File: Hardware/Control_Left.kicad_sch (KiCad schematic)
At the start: 28 parts, among them J1 BAT, J2 JTAG, J3 1.08_MIP_MODULE, Q1 AO3401A, SW1 MSK12C02, SW2 SW_Push, U1 TPS61040DBV, U2 XIAO-NRF52840-PLUS

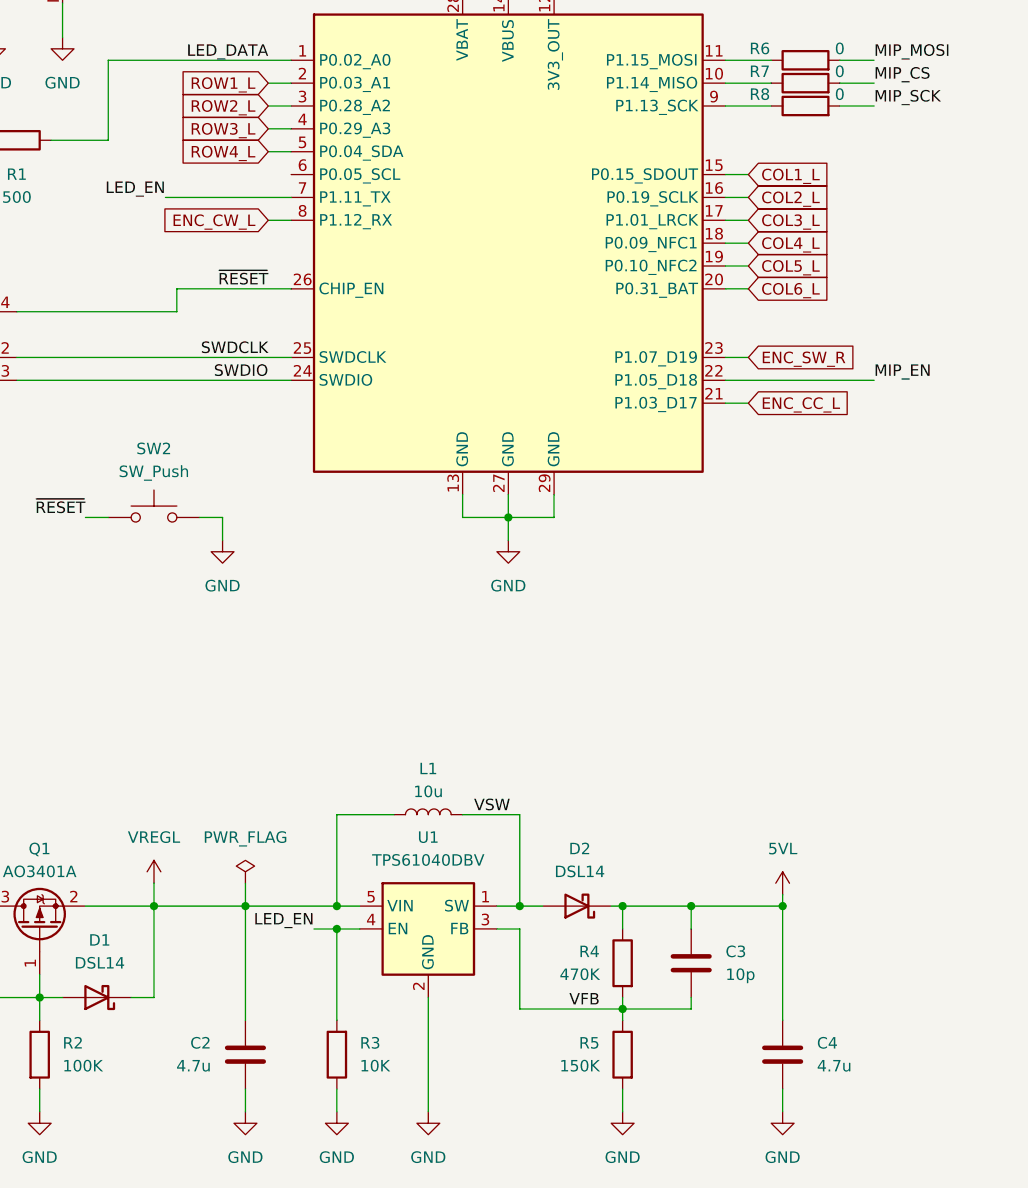
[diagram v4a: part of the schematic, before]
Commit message: Display model and layout
Updated the 3D model and footprint for the MIP display. It now sits further from the PCB.
Continued the layout and routing of the left side PCB.
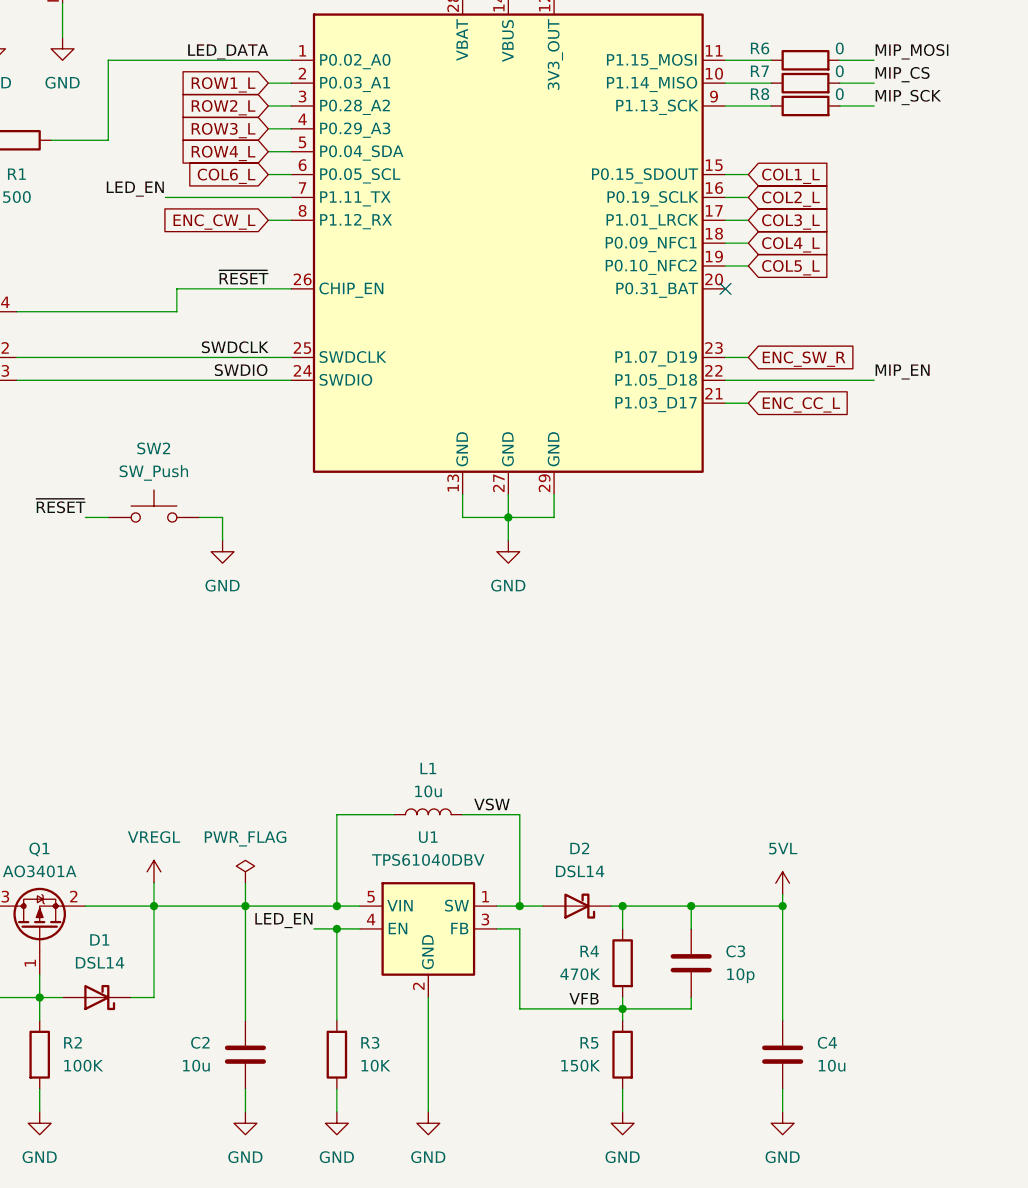
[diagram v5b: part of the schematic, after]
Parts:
- C2, C4: value 4.7u -> 10u; footprint Capacitor_SMD:C_1206_3216Metric -> Capacitor_SMD:C_0603_1608Metric; JLC Part C29823 -> C96446; Manufacturer Part 1206B475K500NT -> CL10A106MA8NRNC
- J3: footprint Custom_Parts:1.08_MIP_MODULE -> Custom_Parts:1.08_MIP_MODULE_TALL
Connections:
- net COL6_L: now also U2.6 (P0.05_SCL); no longer U2.20 (P0.31_BAT)
- no-connect marks 1 -> 2
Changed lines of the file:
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@@
 	)
 	(no_connect
+		(at 138.43 78.74)
+	)
+	(no_connect
 		(at 69.85 43.18)
 	)
@@
 	(wire
 		(pts
+			(xy 87.63 66.04) (xy 90.17 66.04)
+		)
+		(stroke
+			(width 0)
+			(type default)
+		)
+	)
+	(wire
+		(pts
 			(xy 69.85 62.23) (xy 69.85 53.34)
 		)
@@
 	(wire
 		(pts
-			(xy 138.43 78.74) (xy 140.97 78.74)
-		)
-		(stroke
-			(width 0)
-			(type default)
-		)
-	)
-	(wire
-		(pts
 			(xy 217.17 111.76) (xy 234.95 111.76)
 		)
@@
 		)
 	)
-	(global_label "COL6_L"
+	(global_label "ENC_CC_L"
 		(shape input)
-		(at 140.97 78.74 0)
+		(at 140.97 91.44 0)
 		(fields_autoplaced yes)
 		(effects
@@
 		)
 		(property "Intersheetrefs" "${INTERSHEET_REFS}"
-			(at 150.789 78.74 0)
+			(at 153.3894 91.44 0)
 			(hide yes)
 			(show_name no)
@@
 		)
 	)
-	(global_label "ENC_CC_L"
+	(global_label "ROW2_L"
 		(shape input)
-		(at 140.97 91.44 0)
+		(at 87.63 58.42 180)
 		(fields_autoplaced yes)
 		(effects
@@
 				(size 1.27 1.27)
 			)
-			(justify left)
+			(justify right)
 		)
 		(property "Intersheetrefs" "${INTERSHEET_REFS}"
-			(at 153.3894 91.44 0)
+			(at 77.811 58.42 0)
 			(hide yes)
 			(show_name no)
@@
 					(size 1.27 1.27)
 				)
-				(justify left)
+				(justify right)
 			)
 		)
 	)
-	(global_label "ROW2_L"
+	(global_label "ROW4_L"
 		(shape input)
-		(at 87.63 58.42 180)
+		(at 87.63 63.5 180)
 		(fields_autoplaced yes)
 		(effects
@@
 		)
 		(property "Intersheetrefs" "${INTERSHEET_REFS}"
-			(at 77.811 58.42 0)
+			(at 77.811 63.5 0)
 			(hide yes)
 			(show_name no)
@@
 		)
 	)
-	(global_label "ROW4_L"
+	(global_label "ENC_SW_R"
 		(shape input)
-		(at 87.63 63.5 180)
+		(at 140.97 86.36 0)
 		(fields_autoplaced yes)
 		(effects
@@
 				(size 1.27 1.27)
 			)
-			(justify right)
+			(justify left)
 		)
 		(property "Intersheetrefs" "${INTERSHEET_REFS}"
-			(at 77.811 63.5 0)
+			(at 153.5708 86.36 0)
 			(hide yes)
 			(show_name no)
@@
 					(size 1.27 1.27)
 				)
-				(justify right)
+				(justify left)
 			)
 		)
 	)
-	(global_label "ENC_SW_R"
+	(global_label "COL6_L"
 		(shape input)
-		(at 140.97 86.36 0)
+		(at 87.63 66.04 180)
 		(fields_autoplaced yes)
 		(effects
@@
 				(size 1.27 1.27)
 			)
-			(justify left)
+			(justify right)
 		)
 		(property "Intersheetrefs" "${INTERSHEET_REFS}"
-			(at 153.5708 86.36 0)
+			(at 77.811 66.04 0)
 			(hide yes)
 			(show_name no)
@@
 					(size 1.27 1.27)
 				)
-				(justify left)
+				(justify right)
 			)
 		)
@@
 			)
 		)
-		(property "Value" "4.7u"
+		(property "Value" "10u"
 			(at 81.28 165.0999 0)
 			(show_name no)
@@
 			)
 		)
-		(property "Footprint" "Capacitor_SMD:C_1206_3216Metric"
+		(property "Footprint" "Capacitor_SMD:C_0603_1608Metric"
 			(at 84.1248 167.64 0)
 			(hide yes)
@@
 			)
 		)
-		(property "JLC Part" "C29823"
+		(property "JLC Part" "C96446"
 			(at 85.09 163.83 0)
 			(hide yes)
@@
 			)
 		)
-		(property "Manufacturer Part" "1206B475K500NT"
+		(property "Manufacturer Part" "CL10A106MA8NRNC"
 			(at 85.09 163.83 0)
 			(hide yes)
@@
 			)
 		)
-		(property "Footprint" "Custom_Parts:1.08_MIP_MODULE"
+		(property "Footprint" "Custom_Parts:1.08_MIP_MODULE_TALL"
 			(at 238.76 120.65 0)
 			(hide yes)
@@
 			)
 		)
-		(property "Value" "4.7u"
+		(property "Value" "10u"
 			(at 148.59 165.0999 0)
 			(show_name no)
@@
 			)
 		)
-		(property "Footprint" "Capacitor_SMD:C_1206_3216Metric"
+		(property "Footprint" "Capacitor_SMD:C_0603_1608Metric"
 			(at 145.7452 167.64 0)
 			(hide yes)
@@
 			)
 		)
-		(property "JLC Part" "C29823"
+		(property "JLC Part" "C96446"
 			(at 144.78 163.83 0)
 			(hide yes)
@@
 			)
 		)
-		(property "Manufacturer Part" "1206B475K500NT"
+		(property "Manufacturer Part" "CL10A106MA8NRNC"
 			(at 144.78 163.83 0)
 			(hide yes)

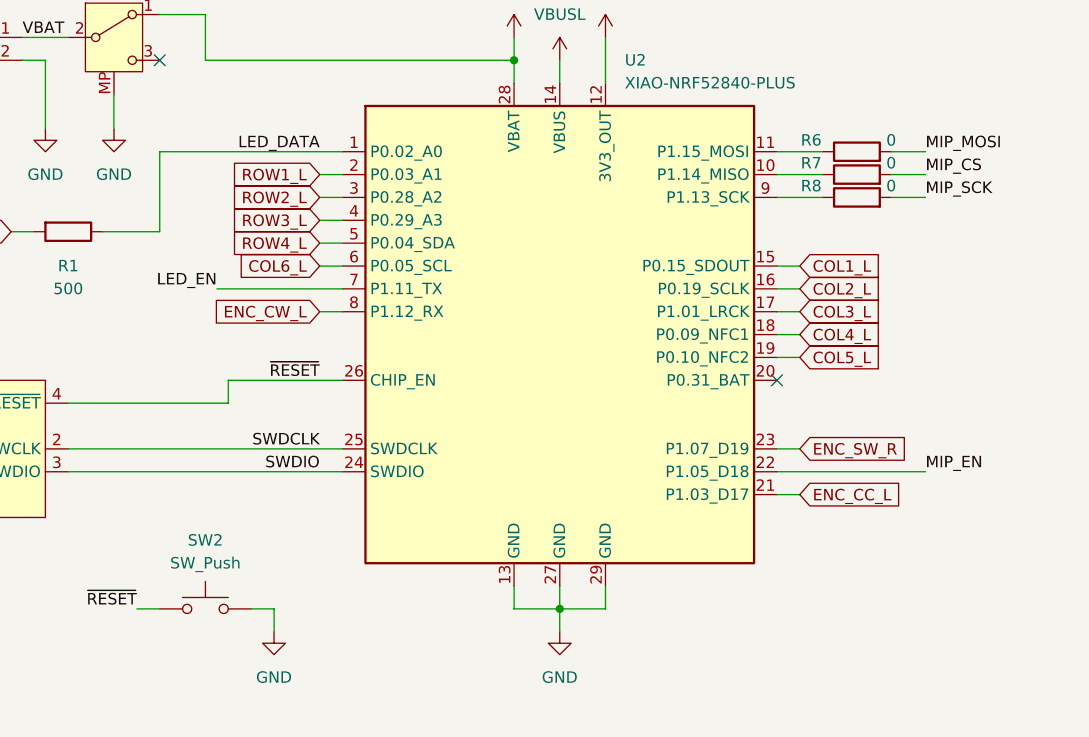
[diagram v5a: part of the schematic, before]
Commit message: Matrix routing and data lines
Routed some of the lines for the switch matrix.
Routed the singal lines for the MIP display.
Need to check clearenaces and spacing between the SPI lines.
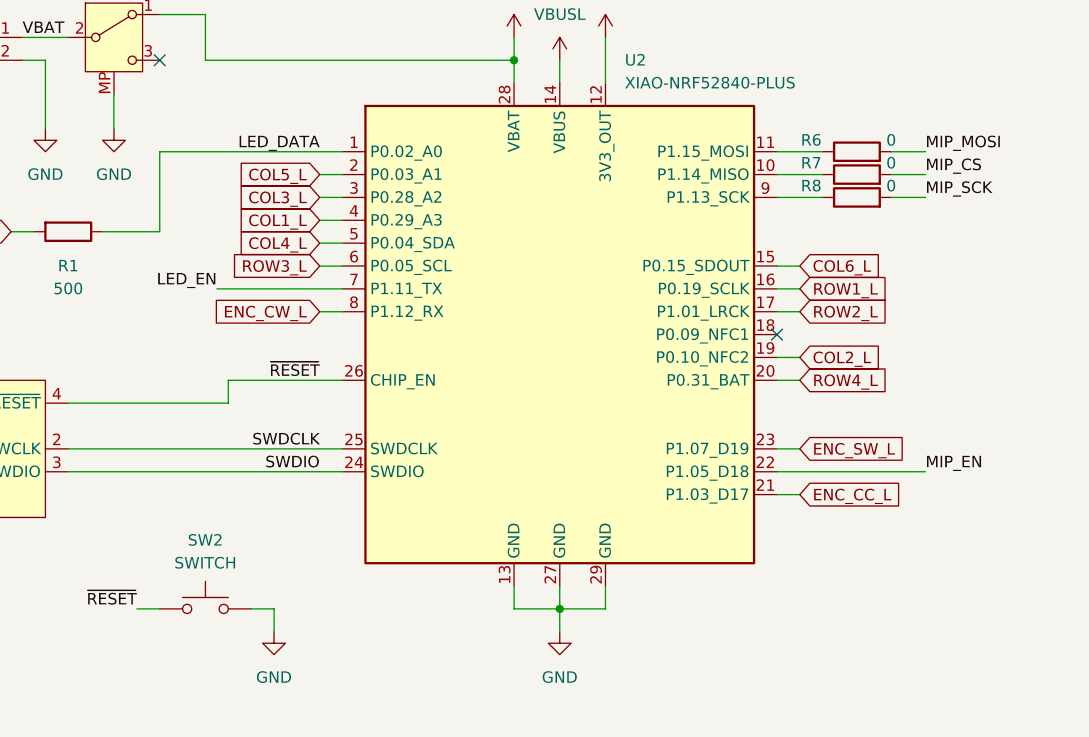
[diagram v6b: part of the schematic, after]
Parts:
- J1: footprint Custom_Parts:JST_PH_1x02_P2.00MM_SMD_HOR -> Custom_Parts:JST_ZH_1x02_P1.50MM_SMD_HORIZONTAL; JLC Part C3029440 -> C722913; Manufacturer Part WAFER-PH2.0-2PWB -> ZH1.5-2P-WT
- SW2: value SW_Push -> SWITCH
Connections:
- net COL1_L: now also U2.4 (P0.29_A3); no longer U2.15 (P0.15_SDOUT)
- net COL2_L: now also U2.19 (P0.10_NFC2); no longer U2.16 (P0.19_SCLK)
- net COL3_L: now also U2.3 (P0.28_A2); no longer U2.17 (P1.01_LRCK)
- net COL4_L: now also U2.5 (P0.04_SDA); no longer U2.18 (P0.09_NFC1)
- net COL5_L: now also U2.2 (P0.03_A1); no longer U2.19 (P0.10_NFC2)
- net COL6_L: now also U2.15 (P0.15_SDOUT); no longer U2.6 (P0.05_SCL)
- net ROW1_L: now also U2.16 (P0.19_SCLK); no longer U2.2 (P0.03_A1)
- net ROW2_L: now also U2.17 (P1.01_LRCK); no longer U2.3 (P0.28_A2)
- net ROW3_L: now also U2.6 (P0.05_SCL); no longer U2.4 (P0.29_A3)
- net ROW4_L: now also U2.20 (P0.31_BAT); no longer U2.5 (P0.04_SDA)
- net ENC_SW_R renamed ENC_SW_L
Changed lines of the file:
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@@
 	)
 	(no_connect
-		(at 138.43 78.74)
+		(at 138.43 73.66)
 	)
 	(no_connect
@@
 	(wire
 		(pts
-			(xy 140.97 73.66) (xy 138.43 73.66)
-		)
-		(stroke
-			(width 0)
-			(type default)
-		)
-	)
-	(wire
-		(pts
 			(xy 54.61 43.18) (xy 57.15 43.18)
 		)
@@
 		)
 	)
+	(wire
+		(pts
+			(xy 138.43 78.74) (xy 140.97 78.74)
+		)
+		(stroke
+			(width 0)
+			(type default)
+		)
+	)
 	(label "MIP_CS"
 		(at 154.94 55.88 0)
@@
 		)
 	)
-	(global_label "ROW1_L"
+	(global_label "ENC_CW_L"
 		(shape input)
-		(at 87.63 55.88 180)
+		(at 87.63 71.12 180)
 		(fields_autoplaced yes)
 		(effects
@@
 		)
 		(property "Intersheetrefs" "${INTERSHEET_REFS}"
-			(at 77.811 55.88 0)
+			(at 75.2106 71.12 0)
 			(hide yes)
 			(show_name no)
@@
 		)
 	)
-	(global_label "ENC_CW_L"
+	(global_label "ENC_CC_L"
 		(shape input)
-		(at 87.63 71.12 180)
+		(at 140.97 91.44 0)
 		(fields_autoplaced yes)
 		(effects
@@
 				(size 1.27 1.27)
 			)
-			(justify right)
+			(justify left)
 		)
 		(property "Intersheetrefs" "${INTERSHEET_REFS}"
-			(at 75.2106 71.12 0)
+			(at 153.3894 91.44 0)
 			(hide yes)
 			(show_name no)
@@
 					(size 1.27 1.27)
 				)
-				(justify right)
+				(justify left)
 			)
 		)
 	)
-	(global_label "ENC_CC_L"
+	(global_label "ROW4_L"
 		(shape input)
-		(at 140.97 91.44 0)
+		(at 140.97 78.74 0)
 		(fields_autoplaced yes)
 		(effects
@@
 		)
 		(property "Intersheetrefs" "${INTERSHEET_REFS}"
-			(at 153.3894 91.44 0)
+			(at 151.2123 78.74 0)
 			(hide yes)
 			(show_name no)
@@
 	(global_label "ROW2_L"
 		(shape input)
-		(at 87.63 58.42 180)
+		(at 140.97 71.12 0)
 		(fields_autoplaced yes)
 		(effects
@@
 				(size 1.27 1.27)
 			)
-			(justify right)
+			(justify left)
 		)
 		(property "Intersheetrefs" "${INTERSHEET_REFS}"
-			(at 77.811 58.42 0)
+			(at 151.2123 71.12 0)
 			(hide yes)
 			(show_name no)
@@
 					(size 1.27 1.27)
 				)
-				(justify right)
+				(justify left)
 			)
 		)
 	)
-	(global_label "ROW4_L"
+	(global_label "ENC_SW_L"
 		(shape input)
-		(at 87.63 63.5 180)
+		(at 140.97 86.36 0)
 		(fields_autoplaced yes)
 		(effects
@@
 				(size 1.27 1.27)
 			)
-			(justify right)
+			(justify left)
 		)
 		(property "Intersheetrefs" "${INTERSHEET_REFS}"
-			(at 77.811 63.5 0)
+			(at 153.3289 86.36 0)
 			(hide yes)
 			(show_name no)
@@
 					(size 1.27 1.27)
 				)
-				(justify right)
+				(justify left)
 			)
 		)
 	)
-	(global_label "ENC_SW_R"
+	(global_label "COL6_L"
 		(shape input)
-		(at 140.97 86.36 0)
+		(at 140.97 66.04 0)
 		(fields_autoplaced yes)
 		(effects
@@
 		)
 		(property "Intersheetrefs" "${INTERSHEET_REFS}"
-			(at 153.5708 86.36 0)
+			(at 151.2123 66.04 0)
 			(hide yes)
 			(show_name no)
@@
 		)
 	)
-	(global_label "COL6_L"
+	(global_label "COL2_L"
 		(shape input)
-		(at 87.63 66.04 180)
+		(at 140.97 76.2 0)
 		(fields_autoplaced yes)
 		(effects
@@
 				(size 1.27 1.27)
 			)
-			(justify right)
+			(justify left)
 		)
 		(property "Intersheetrefs" "${INTERSHEET_REFS}"
-			(at 77.811 66.04 0)
+			(at 151.2123 76.2 0)
 			(hide yes)
 			(show_name no)
@@
 					(size 1.27 1.27)
 				)
-				(justify right)
+				(justify left)
 			)
 		)
 	)
-	(global_label "COL2_L"
+	(global_label "ROW3_L"
 		(shape input)
-		(at 140.97 68.58 0)
+		(at 87.63 66.04 180)
 		(fields_autoplaced yes)
 		(effects
@@
 				(size 1.27 1.27)
 			)
-			(justify left)
+			(justify right)
 		)
 		(property "Intersheetrefs" "${INTERSHEET_REFS}"
-			(at 151.2123 68.58 0)
+			(at 77.811 66.04 0)
 			(hide yes)
 			(show_name no)
@@
 					(size 1.27 1.27)
 				)
-				(justify left)
+				(justify right)
 			)
 		)
 	)
-	(global_label "ROW3_L"
+	(global_label "ROW1_L"
 		(shape input)
-		(at 87.63 60.96 180)
+		(at 140.97 68.58 0)
 		(fields_autoplaced yes)
 		(effects
@@
 				(size 1.27 1.27)
 			)
-			(justify right)
+			(justify left)
 		)
 		(property "Intersheetrefs" "${INTERSHEET_REFS}"
-			(at 77.811 60.96 0)
+			(at 151.2123 68.58 0)
 			(hide yes)
 			(show_name no)
@@
 					(size 1.27 1.27)
 				)
-				(justify right)
+				(justify left)
 			)
 		)
@@
 	(global_label "COL5_L"
 		(shape input)
-		(at 140.97 76.2 0)
+		(at 87.63 55.88 180)
 		(fields_autoplaced yes)
 		(effects
@@
 				(size 1.27 1.27)
 			)
-			(justify left)
+			(justify right)
 		)
 		(property "Intersheetrefs" "${INTERSHEET_REFS}"
-			(at 151.2123 76.2 0)
+			(at 77.811 55.88 0)
 			(hide yes)
 			(show_name no)
@@
 					(size 1.27 1.27)
 				)
-				(justify left)
+				(justify right)
 			)
 		)
@@
 	(global_label "COL4_L"
 		(shape input)
-		(at 140.97 73.66 0)
+		(at 87.63 63.5 180)
 		(fields_autoplaced yes)
 		(effects
@@
 				(size 1.27 1.27)
 			)
-			(justify left)
+			(justify right)
 		)
 		(property "Intersheetrefs" "${INTERSHEET_REFS}"
-			(at 151.2123 73.66 0)
+			(at 77.811 63.5 0)
 			(hide yes)
 			(show_name no)
@@
 					(size 1.27 1.27)
 				)
-				(justify left)
+				(justify right)
 			)
 		)
@@
 	(global_label "COL3_L"
 		(shape input)
-		(at 140.97 71.12 0)
+		(at 87.63 58.42 180)
 		(fields_autoplaced yes)
 		(effects
@@
 				(size 1.27 1.27)
 			)
-			(justify left)
+			(justify right)
 		)
 		(property "Intersheetrefs" "${INTERSHEET_REFS}"
-			(at 151.2123 71.12 0)
+			(at 77.811 58.42 0)
 			(hide yes)
 			(show_name no)
@@
 					(size 1.27 1.27)
 				)
-				(justify left)
+				(justify right)
 			)
 		)
@@
 	(global_label "COL1_L"
 		(shape input)
-		(at 140.97 66.04 0)
+		(at 87.63 60.96 180)
 		(fields_autoplaced yes)
 		(effects
@@
 				(size 1.27 1.27)
 			)
-			(justify left)
+			(justify right)
 		)
 		(property "Intersheetrefs" "${INTERSHEET_REFS}"
-			(at 151.2123 66.04 0)
+			(at 77.811 60.96 0)
 			(hide yes)
 			(show_name no)
@@
 					(size 1.27 1.27)
 				)
-				(justify left)
+				(justify right)
 			)
 		)
@@
 			)
 		)
-		(property "Footprint" "Custom_Parts:JST_PH_1x02_P2.00MM_SMD_HOR"
+		(property "Footprint" "Custom_Parts:JST_ZH_1x02_P1.50MM_SMD_HORIZONTAL"
 			(at 49.53 40.64 0)
 			(hide yes)
@@
 			)
 		)
-		(property "JLC Part" "C3029440"
+		(property "JLC Part" "C722913"
 			(at 49.53 40.64 0)
 			(hide yes)
@@
 			)
 		)
-		(property "Manufacturer Part" "WAFER-PH2.0-2PWB"
+		(property "Manufacturer Part" "ZH1.5-2P-WT"
 			(at 49.53 40.64 0)
 			(hide yes)
@@
 			)
 		)
-		(property "Value" "SW_Push"
+		(property "Value" "SWITCH"
 			(at 74.93 99.06 0)
 			(show_name no)
